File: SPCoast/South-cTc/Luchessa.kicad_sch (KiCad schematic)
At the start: 17 parts, among them SW784 783, SW796 795, SW800 799, U4 0x24, U5 0x25, U6 0x26

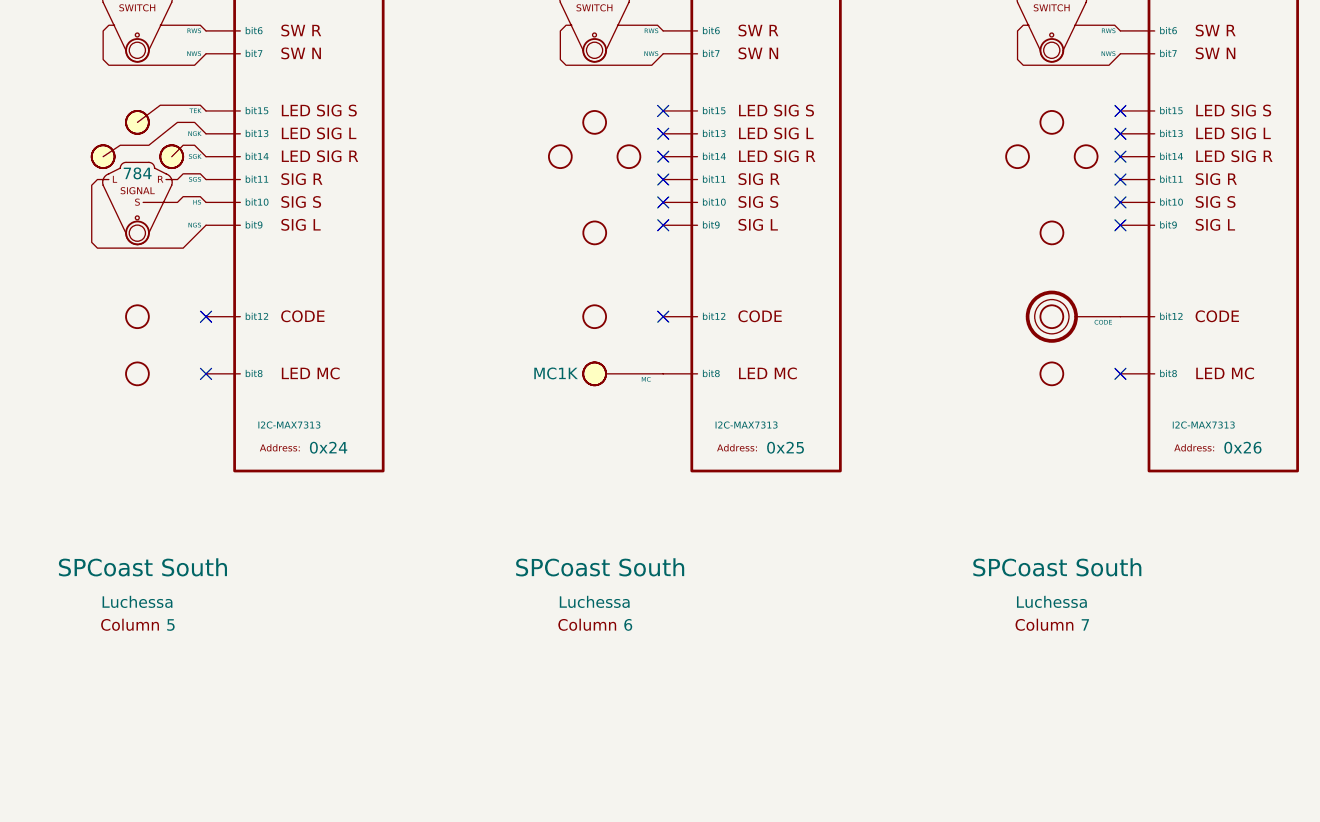
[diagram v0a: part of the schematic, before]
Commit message: feat(kicad): name Luchessa columns' CPs and use PanelMCall for MC1
- Columns 5/6/7 carry CP Name = CP Luchessa / CP Gilroy / CP Carnadero
  (a column IS a CP).
- MC1 is now a PanelMCall (Kind MAINTAINER_CALL) instead of a generic
  PanelAuxiliary.
- Embedded symbol copies updated from RailroadPanel (field values kept).
- Luchessa.kicad_pro: KiCad cleared used_designators on save.

Verified: kicad-cli ERC 0 violations; netlist playtest resolves every
Luchessa appliance to one column and its MAX7313 bits; lamp
IndicationTokens intact.

Co-Authored-By: Claude Opus 5.5 (1M context) <noreply@anthropic.com>
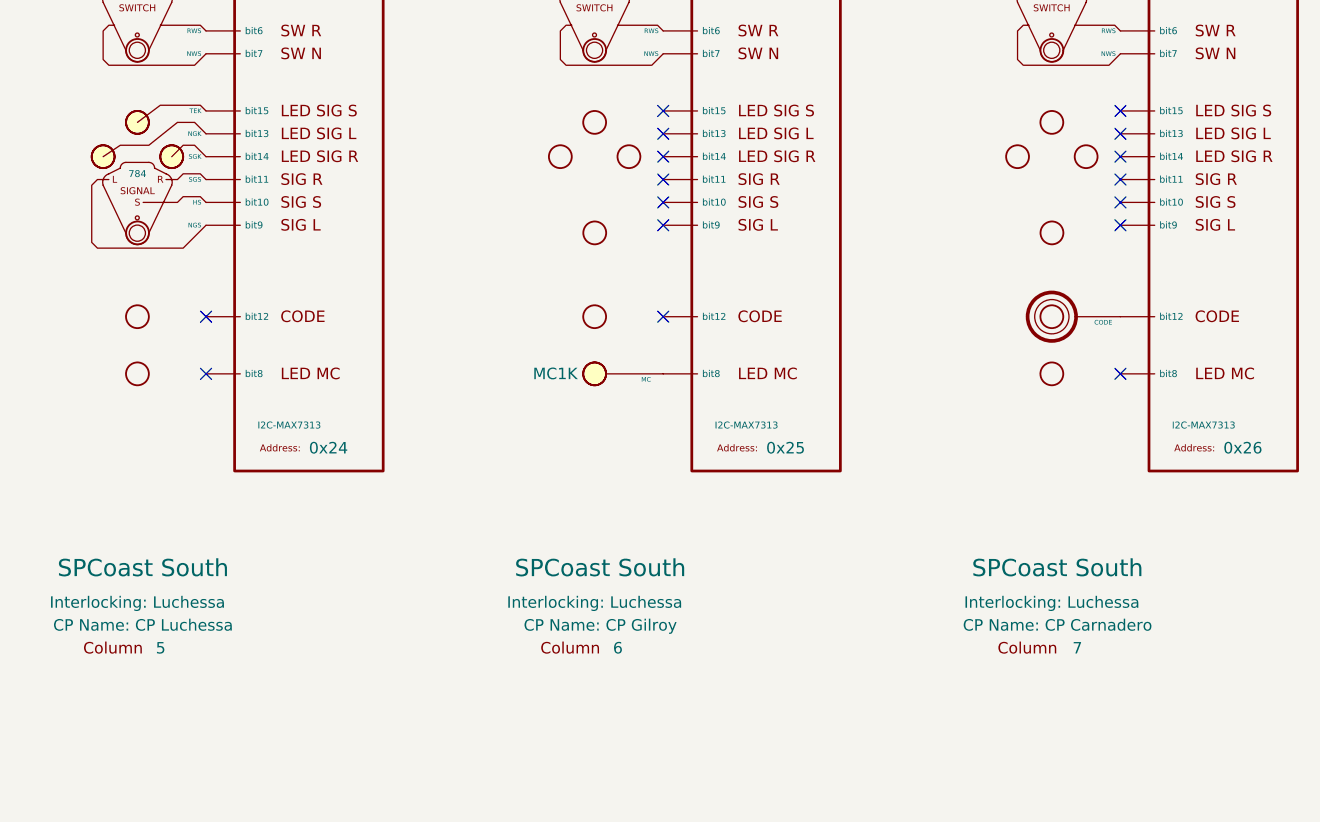
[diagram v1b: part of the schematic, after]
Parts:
- AUX2: symbol RailroadPanel:PanelAuxiliary -> RailroadPanel:PanelMCall
- COL4: CP Name (none) -> CP Luchessa
- COL5: CP Name (none) -> CP Gilroy
- COL6: CP Name (none) -> CP Carnadero
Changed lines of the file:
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@@
 		)
 		(property "Value" "6"
-			(at 133.985 132.08 0)
+			(at 132.842 134.62 0)
 			(show_name no)
 			(do_not_autoplace yes)
@@
 		(property "Interlocking" "Luchessa"
 			(at 130.81 129.54 0)
-			(show_name no)
+			(show_name yes)
 			(do_not_autoplace yes)
 			(effects
@@
 		)
 		(property "Column" "${VALUE}"
-			(at 138.43 134.62 0)
-			(hide yes)
-			(show_name no)
+			(at 133.35 120.65 0)
+			(hide yes)
+			(show_name no)
+			(do_not_autoplace yes)
+			(effects
+				(font
+					(size 1.27 1.27)
+				)
+			)
+		)
+		(property "CP Name" "CP Gilroy"
+			(at 131.445 132.08 0)
+			(show_name yes)
 			(do_not_autoplace yes)
 			(effects
@@
 		)
 		(property "Value" "7"
-			(at 184.785 132.08 0)
+			(at 183.896 134.62 0)
 			(show_name no)
 			(do_not_autoplace yes)
@@
 		(property "Interlocking" "Luchessa"
 			(at 181.61 129.54 0)
-			(show_name no)
+			(show_name yes)
 			(do_not_autoplace yes)
 			(effects
@@
 		)
 		(property "Column" "${VALUE}"
-			(at 189.23 134.62 0)
-			(hide yes)
-			(show_name no)
+			(at 184.15 120.65 0)
+			(hide yes)
+			(show_name no)
+			(do_not_autoplace yes)
+			(effects
+				(font
+					(size 1.27 1.27)
+				)
+			)
+		)
+		(property "CP Name" "CP Carnadero"
+			(at 182.245 132.08 0)
+			(show_name yes)
 			(do_not_autoplace yes)
 			(effects
@@
 	)
 	(symbol
-		(lib_id "RailroadPanel:PanelAuxiliary")
+		(lib_id "RailroadPanel:PanelMCall")
 		(at 130.81 48.26 0)
 		(unit 1)
@@
 			(effects
 				(font
-					(size 1.27 1.27)
+					(size 0.762 0.762)
 				)
 			)
@@
 		)
 		(property "Value" "5"
-			(at 83.185 132.08 0)
+			(at 82.042 134.62 0)
 			(show_name no)
 			(do_not_autoplace yes)
@@
 		(property "Interlocking" "Luchessa"
 			(at 80.01 129.54 0)
-			(show_name no)
+			(show_name yes)
 			(do_not_autoplace yes)
 			(effects
@@
 		)
 		(property "Column" "${VALUE}"
-			(at 87.63 134.62 0)
-			(hide yes)
-			(show_name no)
-			(do_not_autoplace yes)
-			(effects
+			(at 82.55 120.65 0)
+			(hide yes)
+			(show_name no)
+			(do_not_autoplace yes)
+			(effects
+				(font
+					(size 1.27 1.27)
+				)
+			)
+		)
+		(property "CP Name" "CP Luchessa"
+			(at 80.645 132.08 0)
+			(show_name yes)
+			(do_not_autoplace yes)
+			(effects

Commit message: SPCoast: derail pin R, track circuit names end in T, code line symbols on the root sheet
Working-tree changes from the 2026-10-01..03 vocabulary review with
FieldUnit-Subdivision (docs/adr/0001-code-line-type-contract.md):

- Switch_Powered_Derail pin 2 is R (through path = REVERSE) in the seven
  plant schematics (library Railroad.kicad_sym renamed alongside; not in git)
- Luchessa track circuits renamed to end in T (1SAT, 2NAAT, ...); MC1 moved
  to CP Gilroy's house
- South-cTc: transports (MQTT, TimeCode, CMRInet, Loconet) on the root
  sheet on the CtcMachine Transports pin; field stations as encoding
  instances on the Luchessa sheet; two Luchessa lamp tokens renamed
- Six plant projects (Christopher, Corporal, GilroyCalTrain,
  GilroyInterchange, Sargent, Watsonville) added as drawn so far; Watsonville
  updated 2026-10-02

Co-Authored-By: Claude Fable 5.1 <noreply@anthropic.com>
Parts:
- removed CODELINE3: VIRTUAL, symbol RailroadPanel:Codeline-Virtual
- added Encoding2, Encoding3, Encoding4: US&S 506, symbol RailroadPanel:Codeline-Encoding-US&S-506
- added Encoding5, Encoding6: Bit Packing, symbol RailroadPanel:Codeline-Encoding-Bits
- COL4: CP Name CP Luchessa -> Luchessa
- COL5: CP Name CP Gilroy -> Gilroy
- COL6: CP Name CP Carnadero -> Carnadero
- LAMP6: IndicationToken 1NA -> 1NAT
- LAMP7: IndicationToken 795T1,2NAA,799T1 -> 795T1,2NAAT,799T1
- SW796: symbol RailroadPanel:PanelSwitch -> RailroadPanel:PanelLock
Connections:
- new net CMRInet: Encoding5.1 (Encoding)
- new net Loconet: Encoding6.1 (Encoding)
- new net TIMECODE: Encoding2.1 (Encoding), Encoding3.1 (Encoding), Encoding4.1 (Encoding)

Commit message: SPCoast: Address field and Kind on PanelColumn-MAX7313; encoding Values; HBA; Watsonville update
Owner's drawing changes of 2026-10-02..03 (FieldUnit-Subdivision ADR 0002 D18
and the owner's responses):

- PanelColumn-MAX7313: the expander address moves from the Value to an
  Address field (Value is ${Address}); BusKind renamed Kind (I2C-MAX7313)
- Luchessa encoding symbols: Value "US&S 506 time-coded DC pulses"
- Sargent: HBD renamed HBA; traffic indications [NSEW]FLK
- Watsonville schematic brought to a usable state
- Luchessa plant: track circuits end in T; MC1 at CP Gilroy's house

Co-Authored-By: Claude Fable 5.1 <noreply@anthropic.com>
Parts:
- U4: Address (none) -> 0x24; BusKind I2C-MAX7313 -> (none); Kind (none) -> I2C-MAX7313
- U5: Address (none) -> 0x25; BusKind I2C-MAX7313 -> (none); Kind (none) -> I2C-MAX7313
- U6: Address (none) -> 0x26; BusKind I2C-MAX7313 -> (none); Kind (none) -> I2C-MAX7313
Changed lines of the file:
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@@
 			)
 		)
-		(property "Description" "Union Switch & Signal (US&S / USS) Type L Form 506 2-wire time-coded electrical DC pulses"
+		(property "Description" "US&S 506 time-coded pulses"
 			(at 44.45 193.04 0)
 			(hide yes)
@@
 			)
 		)
-		(property "Description" "Union Switch & Signal (US&S / USS) Type L Form 506 2-wire time-coded electrical DC pulses"
+		(property "Description" "US&S 506 time-coded pulses"
 			(at 44.45 184.15 0)
 			(hide yes)
@@
 		(property "Value" "0x24"
 			(at 99.06 112.395 0)
+			(hide yes)
 			(show_name no)
 			(do_not_autoplace yes)
@@
 			)
 		)
-		(property "BusKind" "I2C-MAX7313"
+		(property "Role" "IODRIVER"
+			(at 97.79 107.315 0)
+			(hide yes)
+			(show_name no)
+			(do_not_autoplace no)
+			(effects
+				(font
+					(size 1.27 1.27)
+				)
+			)
+		)
+		(property "Kind" "I2C-MAX7313"
 			(at 93.345 109.855 0)
 			(show_name no)
-			(do_not_autoplace yes)
+			(do_not_autoplace no)
 			(effects
 				(font
@@
 			)
 		)
-		(property "Role" "IODRIVER"
-			(at 99.06 72.39 0)
-			(hide yes)
+		(property "Address" "0x24"
+			(at 101.092 112.522 0)
 			(show_name no)
 			(do_not_autoplace no)
@@
 		(property "Value" "0x26"
 			(at 200.66 112.395 0)
+			(hide yes)
 			(show_name no)
 			(do_not_autoplace yes)
@@
 			)
 		)
-		(property "BusKind" "I2C-MAX7313"
+		(property "Role" "IODRIVER"
+			(at 199.39 107.315 0)
+			(hide yes)
+			(show_name no)
+			(do_not_autoplace no)
+			(effects
+				(font
+					(size 1.27 1.27)
+				)
+			)
+		)
+		(property "Kind" "I2C-MAX7313"
 			(at 194.945 109.855 0)
 			(show_name no)
-			(do_not_autoplace yes)
+			(do_not_autoplace no)
 			(effects
 				(font
@@
 			)
 		)
-		(property "Role" "IODRIVER"
-			(at 200.66 72.39 0)
-			(hide yes)
+		(property "Address" "0x26"
+			(at 202.692 112.522 0)
 			(show_name no)
 			(do_not_autoplace no)
@@
 			)
 		)
-		(property "Description" "Union Switch & Signal (US&S / USS) Type L Form 506 2-wire time-coded electrical DC pulses"
+		(property "Description" "US&S 506 time-coded pulses"
 			(at 44.45 201.93 0)
 			(hide yes)
@@
 		(property "Value" "0x25"
 			(at 149.86 112.395 0)
+			(hide yes)
 			(show_name no)
 			(do_not_autoplace yes)
@@
 			)
 		)
-		(property "BusKind" "I2C-MAX7313"
+		(property "Role" "IODRIVER"
+			(at 148.59 107.315 0)
+			(hide yes)
+			(show_name no)
+			(do_not_autoplace no)
+			(effects
+				(font
+					(size 1.27 1.27)
+				)
+			)
+		)
+		(property "Kind" "I2C-MAX7313"
 			(at 144.145 109.855 0)
 			(show_name no)
-			(do_not_autoplace yes)
+			(do_not_autoplace no)
 			(effects
 				(font
@@
 			)
 		)
-		(property "Role" "IODRIVER"
-			(at 149.86 72.39 0)
-			(hide yes)
-			(show_name no)
-			(do_not_autoplace no)
+		(property "Address" "0x25"
+			(at 151.892 112.268 0)
+			(show_name no)
+			(do_not_autoplace no)

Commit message: fix(kicad): Luchessa circuit 2NAAT becomes 01T
Owner-approved. The circuit lies between the OS circuits of switches 795 and
799 and contains neither, so it takes the zero-prefixed local form 0<n>T. The
desk OS lamp token follows.

Verified: the plant compiles with 01T in the home-clear lists of the same
routes as before; desk lamp tokens read 795T1, 01T, 799T1. FieldUnit-Subdivision
tests, the smoke script and generated JSON still cite 2NAAT; they change in
their own step.

Co-Authored-By: Claude Sonnet 5.5 <noreply@anthropic.com>
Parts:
- LAMP7: IndicationToken 795T1,2NAAT,799T1 -> 795T1,01T,799T1
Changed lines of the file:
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@@
 			)
 		)
-		(property "IndicationToken" "795T1,2NAAT,799T1"
+		(property "IndicationToken" "795T1,01T,799T1"
 			(at 128.905 31.75 0)
 			(show_name no)

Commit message: chore(kicad): sweep instance Role/Kind and stale fields to the library vocabulary
Scripted, one pass over every sheet except Watsonville (open in KiCad, locked):
- Role/Kind of placed symbols refreshed from the library by lib_id: 10 Role
  (MAIN HOUSE CONTROLLED_POINT -> CONTROL_POINT, Rule251-DoT empty) and 17 Kind
  (IRJ-Signal IRJ -> IRJ_SIGNAL x7, Mast_Single/Double swaps, HandThrow
  -> SWITCH_MANUAL, Derail, PanelLock -> LOCK_LEVER, NextCP).
- Stale instance fields dropped where the library no longer has them: 39 Name,
  28 Direction (all empty or retired), 5 CP on Bumper and IRJ symbols.
- Orphan embedded copies of the retired symbol Rule6.28-OtherThanMain removed
  from two sheets (unused).

Not done: Watsonville (locked); CMRInet -> CMRI (library Kind still CMRInet);
fields new to the library (MAIN HOUSE Kind, switch Indications) are not copied
onto instances, the compiler will read library defaults by lib_id; Rulebook
fields stay until the compiler stops requiring them.

Verified: per-symbol before/after comparison shows only these changes, same
symbol sets, positions and lib_ids; netlists keep their net counts (Christopher
33, Corporal 26, GilroyCalTrain 27, GilroyInterchange 22, Luchessa 34, Sargent
18, South-cTc 341); desk still 75 appliances, 137 bindings, 14 columns.

Co-Authored-By: Claude Sonnet 5.5 <noreply@anthropic.com>
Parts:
- SW796: Kind SWITCH_LEVER -> LOCK_LEVER
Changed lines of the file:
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@@
 			)
 		)
-		(property "Kind" "SWITCH_LEVER"
+		(property "Kind" "LOCK_LEVER"
 			(at 131.445 73.025 0)
 			(hide yes)

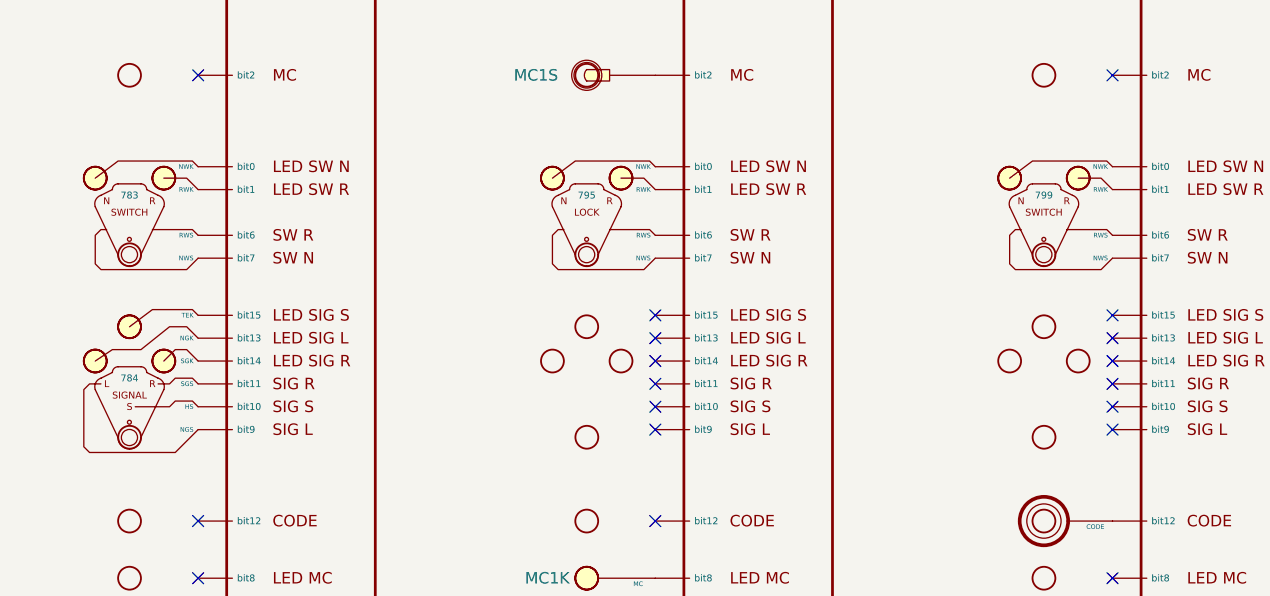
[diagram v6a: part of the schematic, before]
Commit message: chore(kicad): refresh instances to the ADR 0003 libraries (InterlockingPlant 95f53e2)
- Desk sheets (South-cTc/*) and the Sargent sandbox: embedded PanelSwitch, PanelLock,
  PanelSignal, PanelMCall, PanelCode, PanelLamp-*, PanelColumn-MAX7313 definitions refreshed
  from the library (refresh_embedded.py, checked against the pre-pass library: only Description
  text had drifted). Instance Role APPLIANCE -> PANEL (77).
- Plant sheets: powered-switch instance Kind SWITCH_POWERED -> SWITCH_REMOTE (21), matching the
  library (sweep_role_kind_fields.py).

Verified:
- verify_symbol_diff.py: same symbols, lib_ids and positions; only Role/Kind changed.
- Nets unchanged: Christopher 30, Corporal 27, GilroyCalTrain 28, GilroyInterchange 23,
  Luchessa 35, Sargent 61, Watsonville 99, South-cTc 341.
- parse_kicad_plant.py --format text identical before/after for all seven plants.
- Desk compile 75/137/14, diagnostics identical; the 7 desk locks bind WLS/~{WLS}/~{WLK}/WLK
  to the bits that were NWS/RWS/RWK/NWK.
- No sheet or project outside Luchessa carries the copied root UUID.

Co-Authored-By: Claude Opus 5.5 <noreply@anthropic.com>
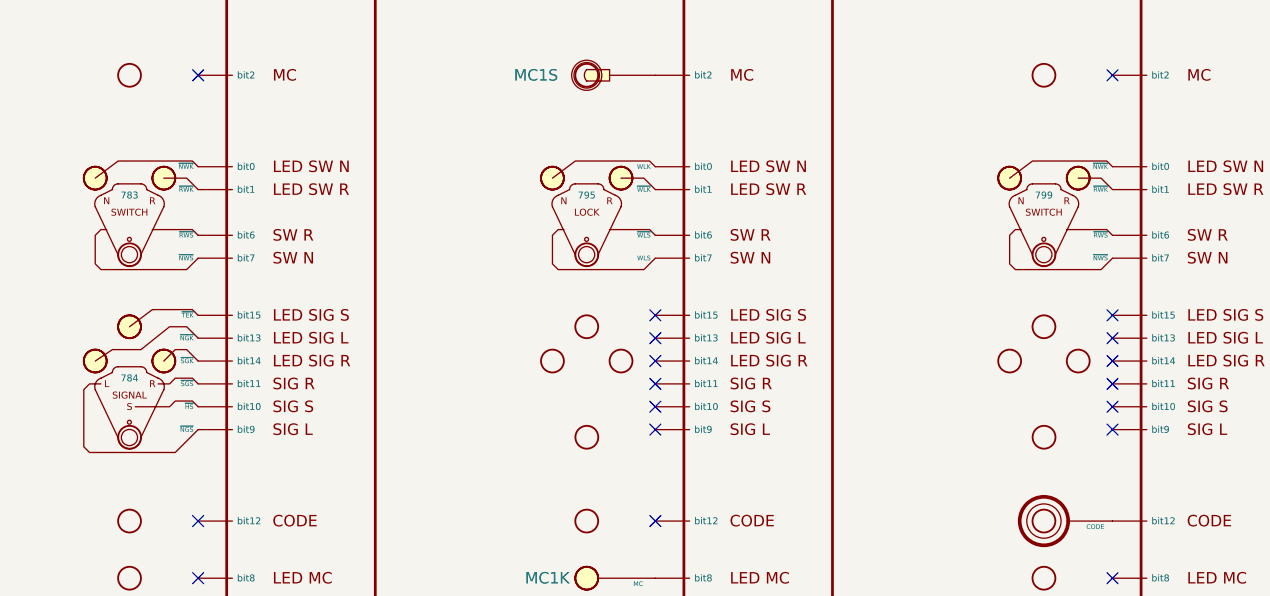
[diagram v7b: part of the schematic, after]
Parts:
- AUX2, CODE2, LAMP5, LAMP6, LAMP7, LAMP8, SIG785, SW784, SW796, SW800: Role APPLIANCE -> PANEL
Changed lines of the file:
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@@
 			)
 		)
-		(property "Role" "APPLIANCE"
+		(property "Role" "PANEL"
 			(at 130.81 101.6 0)
 			(hide yes)
@@
 			)
 		)
-		(property "Role" "APPLIANCE"
+		(property "Role" "PANEL"
 			(at 131.445 74.93 0)
 			(hide yes)
@@
 			)
 		)
-		(property "Role" "APPLIANCE"
+		(property "Role" "PANEL"
 			(at 80.01 29.21 0)
 			(hide yes)
@@
 			)
 		)
-		(property "Role" "APPLIANCE"
+		(property "Role" "PANEL"
 			(at 80.645 76.2 0)
 			(hide yes)
@@
 			)
 		)
-		(property "Role" "APPLIANCE"
+		(property "Role" "PANEL"
 			(at 130.81 24.13 0)
 			(hide yes)
@@
 			)
 		)
-		(property "Role" "APPLIANCE"
+		(property "Role" "PANEL"
 			(at 181.61 90.17 0)
 			(hide yes)
@@
 			)
 		)
-		(property "Role" "APPLIANCE"
+		(property "Role" "PANEL"
 			(at 182.245 76.2 0)
 			(hide yes)
@@
 			)
 		)
-		(property "Role" "APPLIANCE"
+		(property "Role" "PANEL"
 			(at 137.16 44.45 0)
 			(hide yes)
@@
 			)
 		)
-		(property "Role" "APPLIANCE"
+		(property "Role" "PANEL"
 			(at 130.81 34.29 0)
 			(hide yes)
@@
 			)
 		)
-		(property "Role" "APPLIANCE"
+		(property "Role" "PANEL"
 			(at 80.01 92.71 0)
 			(hide yes)

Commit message: chore(kicad): desk sheets to Driver-I2C-MAX7313 and the PanelLock Kind (InterlockingPlant owner review)
- 14 desk expanders: lib_id RailroadPanel:PanelColumn-MAX7313 -> Driver-I2C-MAX7313, embedded
  definition refreshed (pins A1..B8, same numbers and positions).
- 8 PanelLock instances: Kind LOCK_LEVER -> LOCK_LEVER_2LAMP_2CONTACT (7 desk, 1 Sargent sandbox).

Verified:
- verify_symbol_diff.py: only those lib_id and Kind changes.
- South-cTc 341 nets, Sargent 61; desk compile 75/137/14 with bindings identical to e2c1093.

Co-Authored-By: Claude Opus 5.5 <noreply@anthropic.com>
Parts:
- SW796: Kind LOCK_LEVER -> LOCK_LEVER_2LAMP_2CONTACT
- U4, U5, U6: symbol RailroadPanel:PanelColumn-MAX7313 -> RailroadPanel:Driver-I2C-MAX7313
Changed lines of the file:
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@@
 			)
 		)
-		(property "Kind" "LOCK_LEVER"
+		(property "Kind" "LOCK_LEVER_2LAMP_2CONTACT"
 			(at 131.445 73.025 0)
 			(hide yes)
@@
 	)
 	(symbol
-		(lib_id "RailroadPanel:PanelColumn-MAX7313")
+		(lib_id "RailroadPanel:Driver-I2C-MAX7313")
 		(at 99.06 72.39 0)
 		(unit 1)
@@
 	)
 	(symbol
-		(lib_id "RailroadPanel:PanelColumn-MAX7313")
+		(lib_id "RailroadPanel:Driver-I2C-MAX7313")
 		(at 200.66 72.39 0)
 		(unit 1)
@@
 	)
 	(symbol
-		(lib_id "RailroadPanel:PanelColumn-MAX7313")
+		(lib_id "RailroadPanel:Driver-I2C-MAX7313")
 		(at 149.86 72.39 0)
 		(unit 1)
